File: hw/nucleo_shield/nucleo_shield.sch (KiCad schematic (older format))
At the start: 4 parts, among them CN101 Nucleo-F411RE-CN10, CN71 Nucleo-F411RE-CN7, U1 74HC595, U2 74HC595

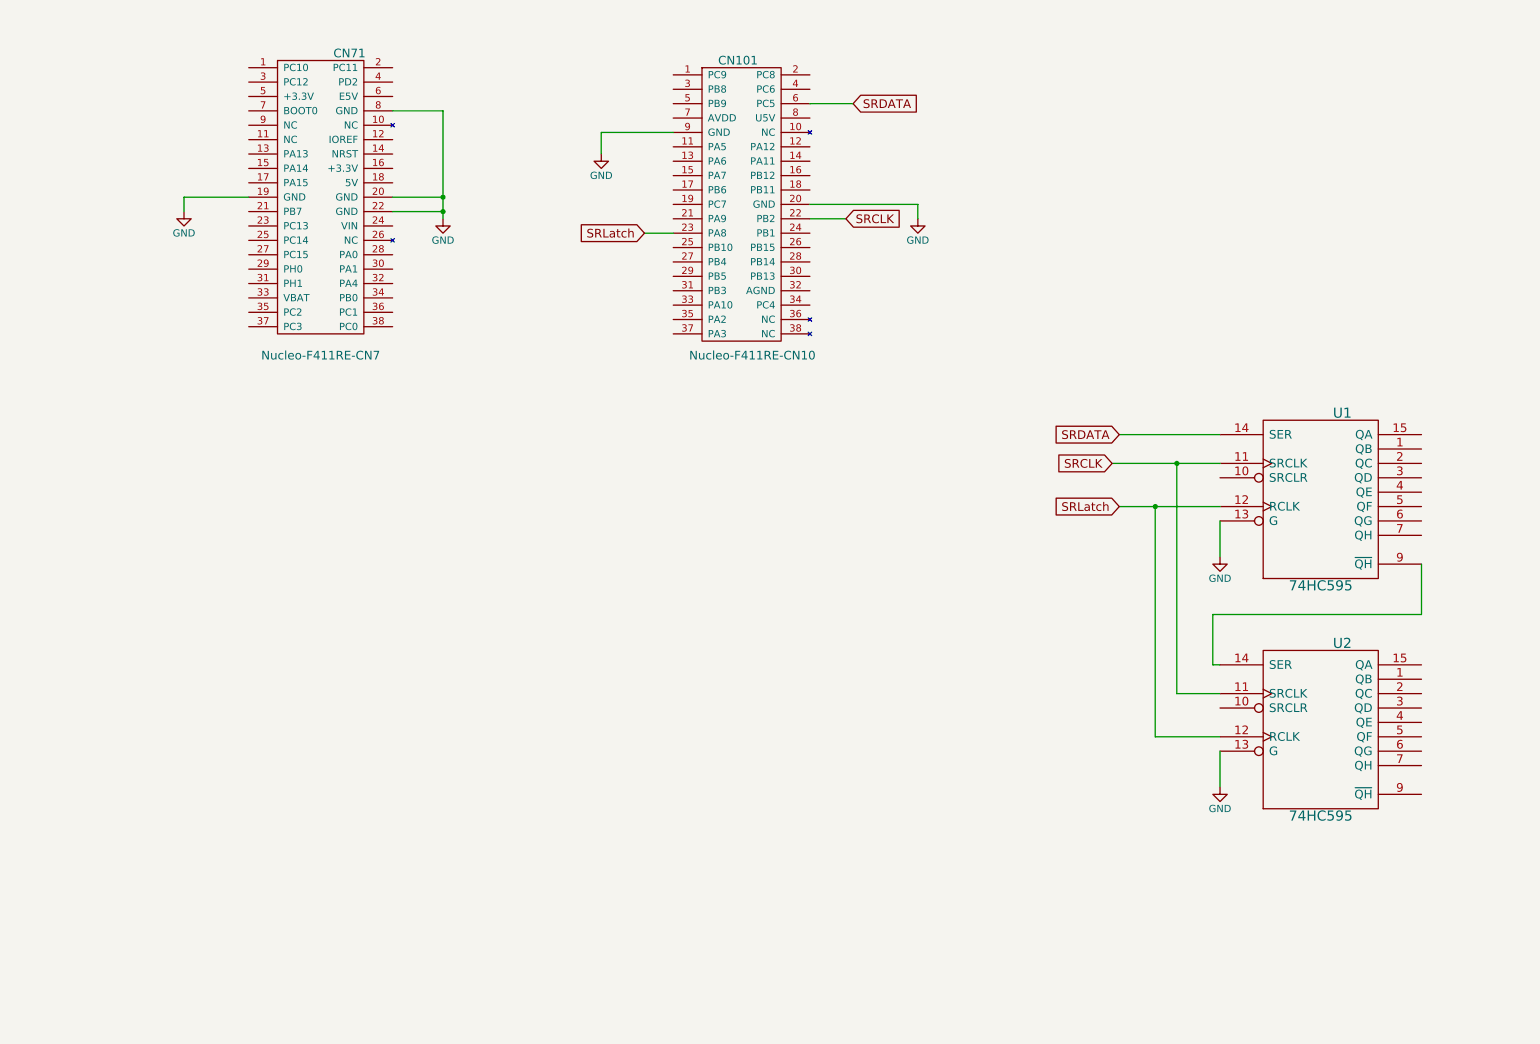
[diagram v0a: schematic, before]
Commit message: Nucleo shield: continue schema by adding optoisolated input
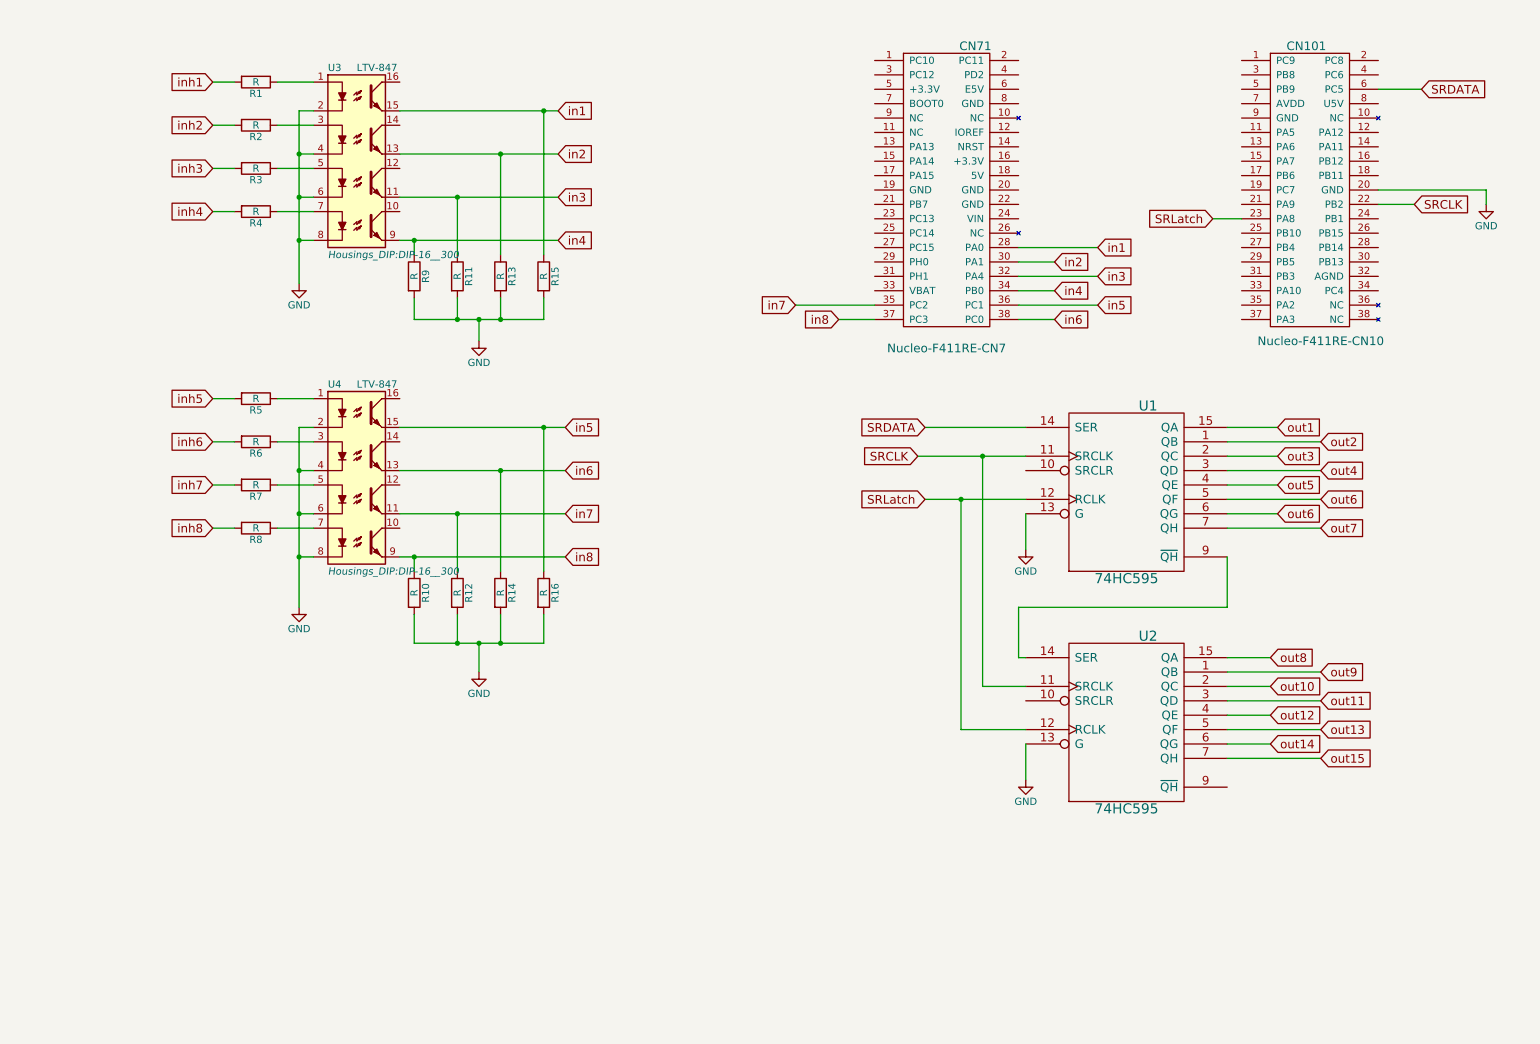
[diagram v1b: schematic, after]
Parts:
- added R1, R10, R11, R12, R13, R14, R15, R16, R2, R3, R4, R5, R6, R7, R8, R9: R, Resistors_ThroughHole:Resistor_Horizontal_RM10mm, symbol R
- added U3, U4: LTV-847, Housings_DIP:DIP-16__300, symbol LTV-847
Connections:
- net GND: now also R10.2, R11.2, R12.2, R13.2, R14.2, R15.2, R16.2, R9.2, U3.2, U3.4, U3.6, U3.8, U4.2, U4.4, U4.6, U4.8; no longer CN101.9 (GND), CN71.19 (GND), CN71.20 (GND), CN71.22 (GND), CN71.8 (GND)
- net in1: now reaches CN71.28 (PA0)
- net in1: now also R15.1, U3.15
- net in2: now reaches CN71.30 (PA1)
- net in2: now also R13.1, U3.13
- net in3: now reaches CN71.32 (PA4)
- net in3: now also R11.1, U3.11
- net in4: now reaches CN71.34 (PB0)
- net in4: now also R9.1, U3.9
- net in7: now reaches CN71.35 (PC2)
- net in7: now also R12.1, U4.11
- net in5: now reaches CN71.36 (PC1)
- net in5: now also R16.1, U4.15
- net in8: now reaches CN71.37 (PC3)
- net in8: now also R10.1, U4.9
- net in6: now reaches CN71.38 (PC0)
- net in6: now also R14.1, U4.13
- net out2: now reaches U1.1 (QB)
- net out1: now reaches U1.15 (QA)
- net out3: now reaches U1.2 (QC)
- net out4: now reaches U1.3 (QD)
- net out5: now reaches U1.4 (QE)
- net out6: now reaches U1.5 (QF)
- net out6: now also U1.6 (QG)
- net out7: now reaches U1.7 (QH)
- net out9: now reaches U2.1 (QB)
- net out8: now reaches U2.15 (QA)
- net out10: now reaches U2.2 (QC)
- net out11: now reaches U2.3 (QD)
- net out12: now reaches U2.4 (QE)
- net out13: now reaches U2.5 (QF)
- net out14: now reaches U2.6 (QG)
- net out15: now reaches U2.7 (QH)
- new net: R1.1, U3.1
- new net: R2.1, U3.3
- new net: R3.1, U3.5
- new net: R4.1, U3.7
- new net: R5.1, U4.1
- new net: R6.1, U4.3
- new net: R7.1, U4.5
- new net: R8.1, U4.7
- new net inh1: R1.2
- new net inh2: R2.2
- new net inh3: R3.2
- new net inh4: R4.2
- new net inh5: R5.2
- new net inh6: R6.2
- new net inh7: R7.2
- new net inh8: R8.2
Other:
- moved on the sheet: CN101, CN71, U1, U2

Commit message: Nucleo: more advance schematic, 8 input, 16 outputs
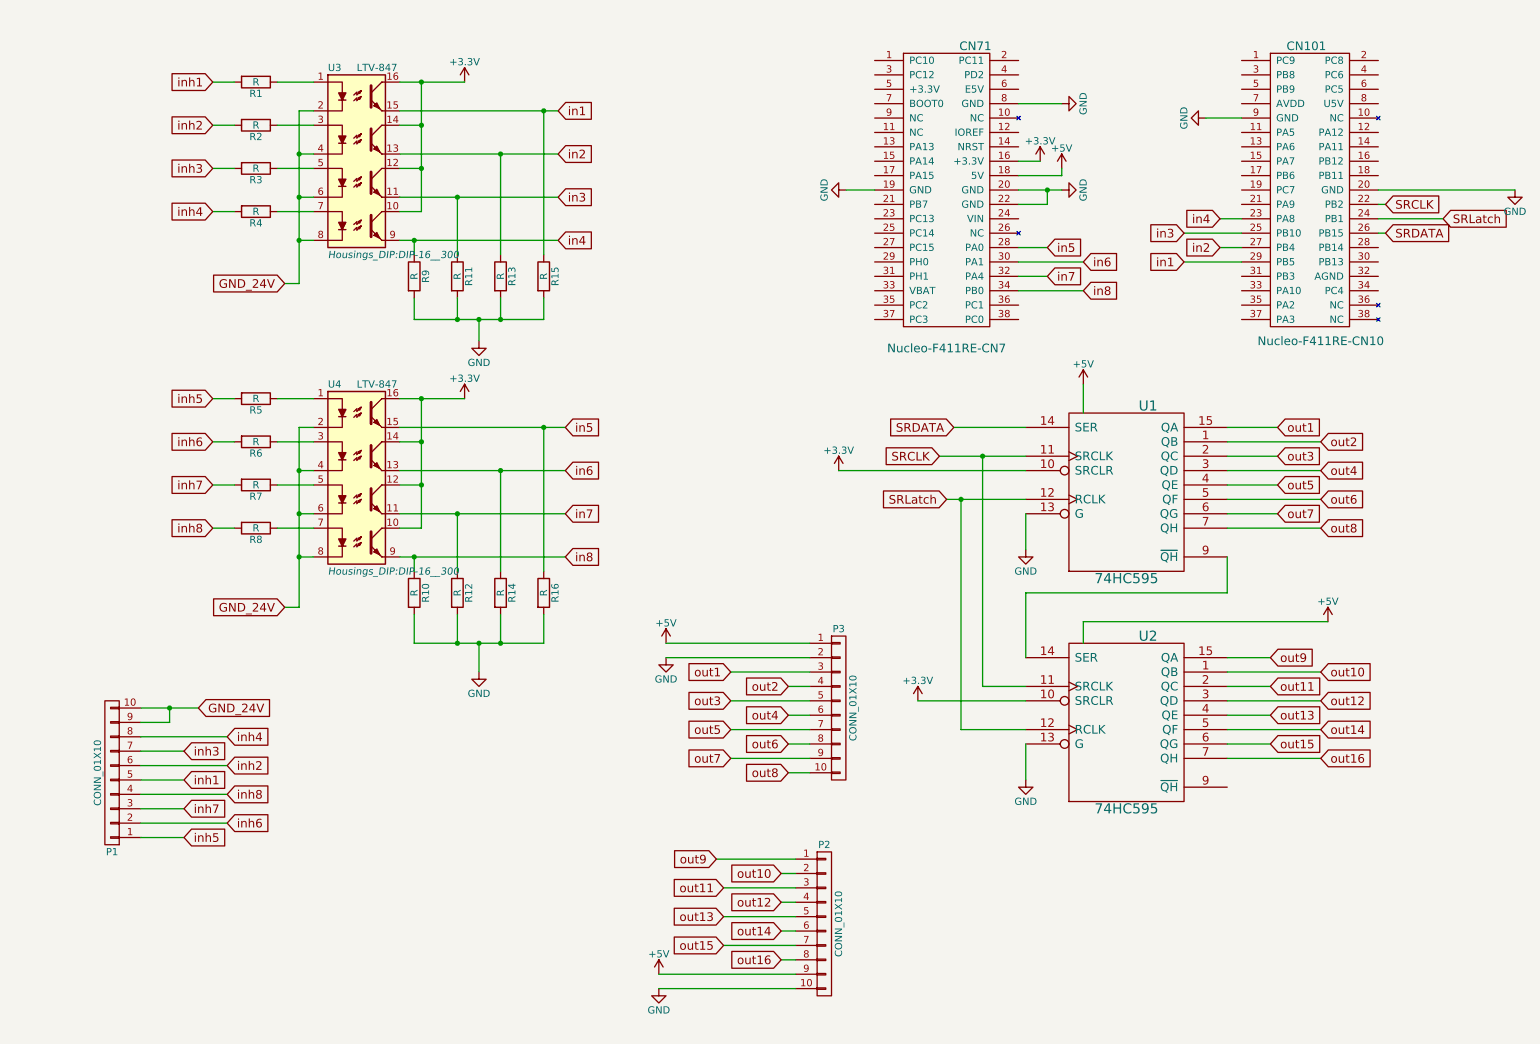
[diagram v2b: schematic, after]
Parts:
- added P1, P2, P3: CONN_01X10, w_conn_screw:mors_10p, symbol CONN_01X10
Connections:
- net VCC is gone; now on net +5V: U1.16 (VCC), U2.16 (VCC)
- net GND: now also CN101.9 (GND), CN71.19 (GND), CN71.20 (GND), CN71.22 (GND), CN71.8 (GND), P2.10 (P10), P3.2 (P2); no longer U3.2, U3.4, U3.6, U3.8, U4.2, U4.4, U4.6, U4.8
- net SRDATA: now also CN101.26 (PB15); no longer CN101.6 (PC5)
- net SRLatch: now also CN101.24 (PB1); no longer CN101.23 (PA8)
- net in1: now also CN101.29 (PB5); no longer CN71.28 (PA0)
- net in2: now also CN101.27 (PB4); no longer CN71.30 (PA1)
- net in3: now also CN101.25 (PB10); no longer CN71.32 (PA4)
- net in4: now also CN101.23 (PA8); no longer CN71.34 (PB0)
- net in5: now also CN71.28 (PA0); no longer CN71.36 (PC1)
- net in6: now also CN71.30 (PA1); no longer CN71.38 (PC0)
- net in7: now also CN71.32 (PA4); no longer CN71.35 (PC2)
- net in8: now also CN71.34 (PB0); no longer CN71.37 (PC3)
- net inh1: now also P1.5 (P5)
- net inh2: now also P1.6 (P6)
- net inh3: now also P1.7 (P7)
- net inh4: now also P1.8 (P8)
- net inh5: now also P1.1 (P1)
- net inh6: now also P1.2 (P2)
- net inh7: now also P1.3 (P3)
- net inh8: now also P1.4 (P4)
- net out1: now also P3.3 (P3)
- net out10: now also U2.1 (QB), P2.2 (P2); no longer U2.2 (QC)
- net out11: now also U2.2 (QC), P2.3 (P3); no longer U2.3 (QD)
- net out12: now also U2.3 (QD), P2.4 (P4); no longer U2.4 (QE)
- net out13: now also U2.4 (QE), P2.5 (P5); no longer U2.5 (QF)
- net out14: now also U2.5 (QF), P2.6 (P6); no longer U2.6 (QG)
- net out15: now also U2.6 (QG), P2.7 (P7); no longer U2.7 (QH)
- net out2: now also P3.4 (P4)
- net out3: now also P3.5 (P5)
- net out4: now also P3.6 (P6)
- net out5: now also P3.7 (P7)
- net out6: now also P3.8 (P8); no longer U1.6 (QG)
- net out7: now also U1.6 (QG), P3.9 (P9); no longer U1.7 (QH)
- net out8: now also U1.7 (QH), P3.10 (P10); no longer U2.15 (QA)
- net out9: now also U2.15 (QA), P2.1 (P1); no longer U2.1 (QB)
- net +3V3: now reaches CN71.16 (+3.3V)
- net +3V3: now also U1.10 (SRCLR), U2.10 (SRCLR), U3.10, U3.12, U3.14, U3.16, U4.10, U4.12, U4.14, U4.16
- net +5V: now reaches CN71.18 (5V)
- net +5V: now also P2.9 (P9), P3.1 (P1)
- new net GND_24V: P1.10 (P10), P1.9 (P9), U3.2, U3.4, U3.6, U3.8, U4.2, U4.4, U4.6, U4.8
- new net out16: P2.8 (P8), U2.7 (QH)

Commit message: Nucleo: fix schematic and pcb
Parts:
- added P4: CONN_01X02, w_conn_screw:mors_2p, symbol CONN_01X02
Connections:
- net +5V: now also CN71.6 (E5V), P4.1 (P1)
- net GND: now also P4.2 (P2)
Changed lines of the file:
@@
 Wire Wire Line
 	9050 4650 9050 4400
+$Comp
+L +5V #PWR022
+U 1 1 56AB5C14
+P 7900 1100
+F 0 "#PWR022" H 7900 950 50  0001 C CNN
+F 1 "+5V" H 7900 1240 50  0000 C CNN
+F 2 "" H 7900 1100 60  0000 C CNN
+F 3 "" H 7900 1100 60  0000 C CNN
+	1    7900 1100
+	1    0    0    -1
+$EndComp
+Wire Wire Line
+	7600 1150 7900 1150
+Wire Wire Line
+	7900 1150 7900 1100
+$Comp
+L CONN_01X02 P4
+U 1 1 56AB61A1
+P 4050 6500
+F 0 "P4" H 4050 6650 50  0000 C CNN
+F 1 "CONN_01X02" V 4150 6500 50  0000 C CNN
+F 2 "w_conn_screw:mors_2p" H 4050 6500 60  0001 C CNN
+F 3 "" H 4050 6500 60  0000 C CNN
+	1    4050 6500
+	1    0    0    -1
+$EndComp
+$Comp
+L +5V #PWR023
+U 1 1 56AB6530
+P 3850 6350
+F 0 "#PWR023" H 3850 6200 50  0001 C CNN
+F 1 "+5V" H 3850 6490 50  0000 C CNN
+F 2 "" H 3850 6350 60  0000 C CNN
+F 3 "" H 3850 6350 60  0000 C CNN
+	1    3850 6350
+	1    0    0    -1
+$EndComp
+$Comp
+L GND #PWR024
+U 1 1 56AB6589
+P 3850 6700
+F 0 "#PWR024" H 3850 6450 50  0001 C CNN
+F 1 "GND" H 3850 6550 50  0000 C CNN
+F 2 "" H 3850 6700 60  0000 C CNN
+F 3 "" H 3850 6700 60  0000 C CNN
+	1    3850 6700
+	1    0    0    -1
+$EndComp
+Wire Wire Line
+	3850 6450 3850 6350
+Wire Wire Line
+	3850 6550 3850 6700
 $EndSCHEMATC
